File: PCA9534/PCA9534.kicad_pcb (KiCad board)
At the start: 2 copper layers, 29.2 x 15.2 mm, 22 parts, among them J1 Conn_01x08, J2 Conn_01x08

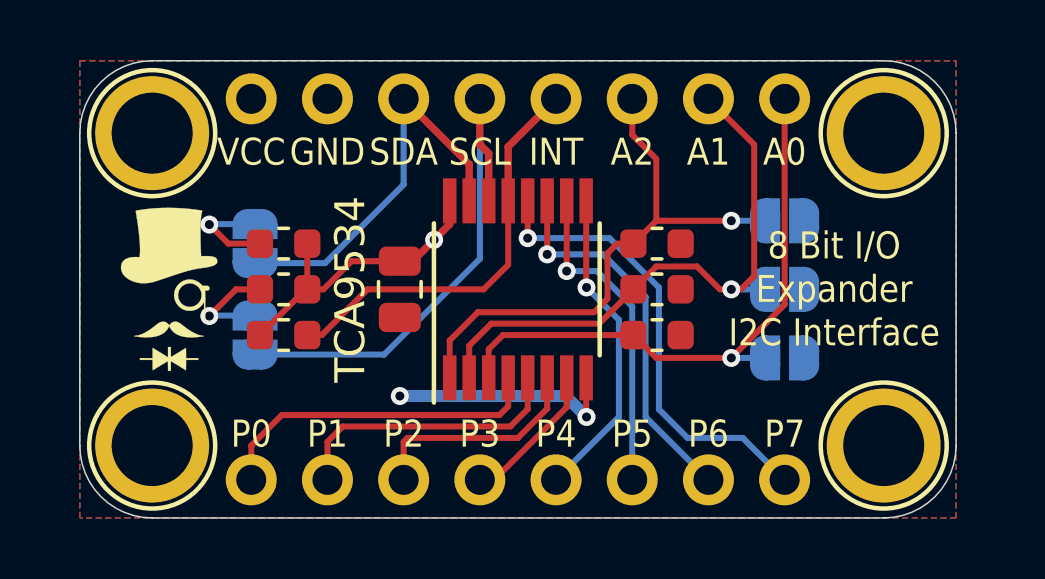
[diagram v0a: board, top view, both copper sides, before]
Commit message: Board Size Updated
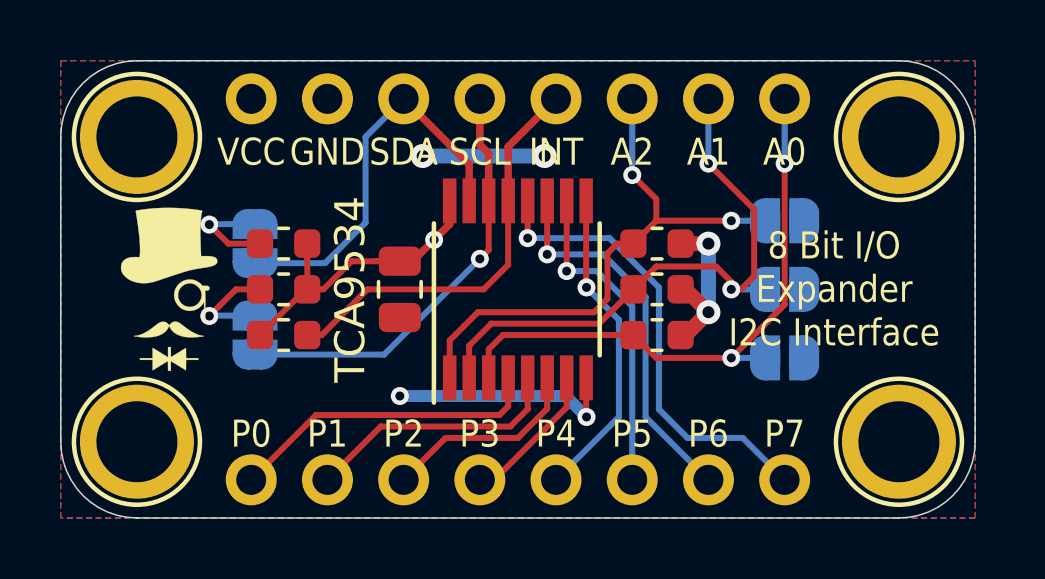
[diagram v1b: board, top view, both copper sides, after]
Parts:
- moved H1 0.52 mm to (49.4, 40.9)
- moved H2 0.52 mm to (49.4, 30.7)
- moved H3 0.52 mm to (74.8, 40.9)
- moved H4 0.52 mm to (74.8, 30.7)
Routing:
- net GND: track 7.82 -> 17.6 mm, vias 2 -> 6
- net SCL: track 17.7 -> 14.4 mm, vias 0 -> 1
- net P2: track 7.54 -> 6.80 mm
- net P1: track 9.44 -> 8.69 mm
- net P0: track 11.2 -> 10.5 mm
- net A1: track 19.8 -> 20.0 mm, vias 1 -> 2
- net A2: vias 1 -> 2
- net A0: vias 1 -> 2
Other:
- board size 29.2 x 15.2 mm -> 30.5 x 15.2 mm
